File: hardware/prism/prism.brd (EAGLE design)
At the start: 100 x 79 mm, 174 parts, among them IC1 XMEGA128-A1, IC2 74LVC4245APW, IC3 LM2731XMF, IC4 74LVC4245APW, IC5 LM25011MY, IC6 NCV78M05BDTRKG, IC7 NRF24L01+, IC8 MAX3232CSE, T1 MMBT2222LT1G, T2 NTGS4111PT1G, T3 MMBT2222LT1G, T4 MMBT2222LT1G, T5 NTGS4111PT1G, T6 MMBT2222LT1G, T7 MMBT2222LT1G, T8 NTGS4111PT1G

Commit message: few changes on board
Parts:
- added R74, R75: 270-E, robotter_resistor:R0805
- R29, R34: value 4K7-E -> 8K2-E
- R36, R41: value nc -> 3K09-F; device rcl:R0603 -> robotter_resistor:R0603
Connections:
- net +3V3: now also R74.2, R75.2
- net IR_SENSOR_0_OUTPUT_3V3: now also R74.1
- net IR_SENSOR_1_OUTPUT_3V3: now also R75.1
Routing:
- net +3V3: track 398.1 -> 401.1 mm, vias 23 -> 24
- net INT0_0_3V3: track 32.4 -> 31.5 mm
- net INT1_0_3V3: track 30.8 -> 30.2 mm
- net INT0_1_3V3: track 31.3 -> 30.7 mm
- net IR_SENSOR_1_OUTPUT_3V3: track 125.6 -> 126.2 mm

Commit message: mouser component ref added
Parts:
- IC6: device linear:DPACK_3 -> robotter_ic:DPACK_3
- MOT0, MOT1: device con-molex:6410-02 -> robotter_connector:6410-02

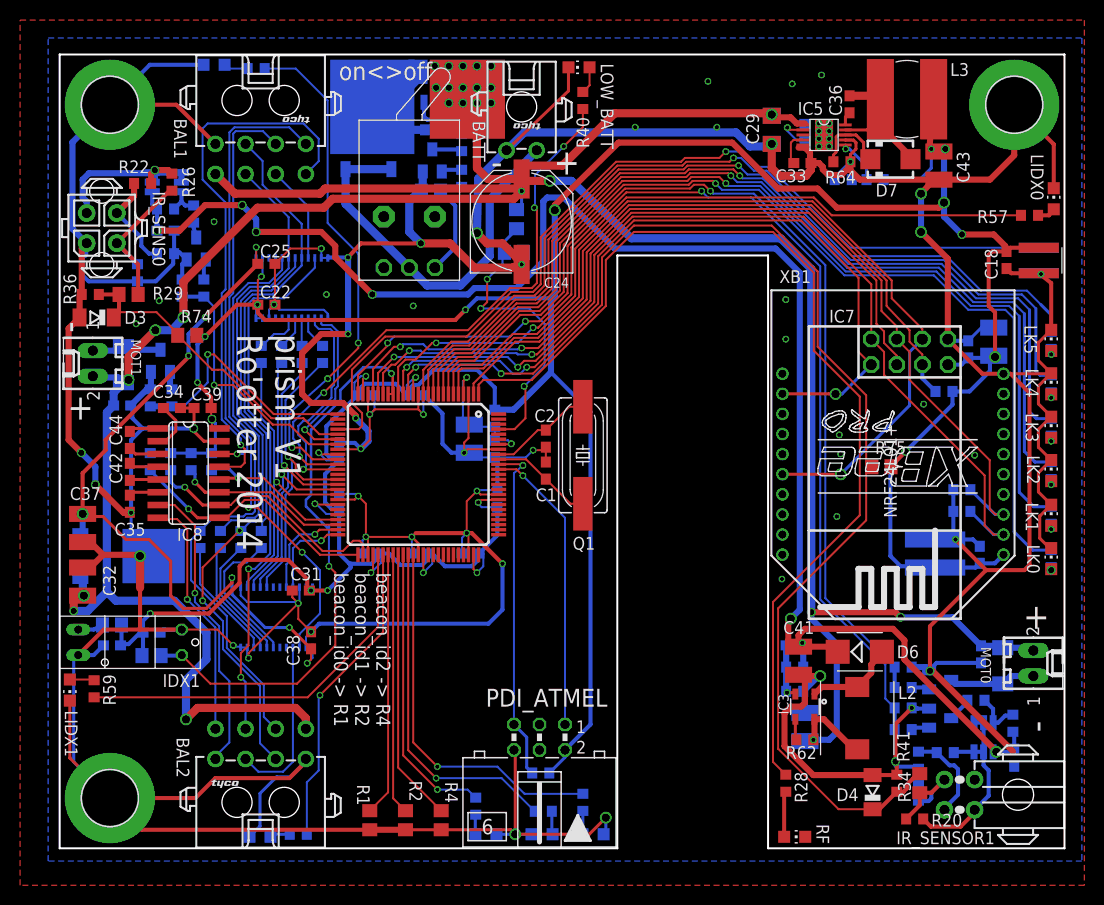
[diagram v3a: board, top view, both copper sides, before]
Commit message: prism v2 : modifications after beacon integration : mirror motor supplied by vbat or +15V, diode B160 pinout corrected
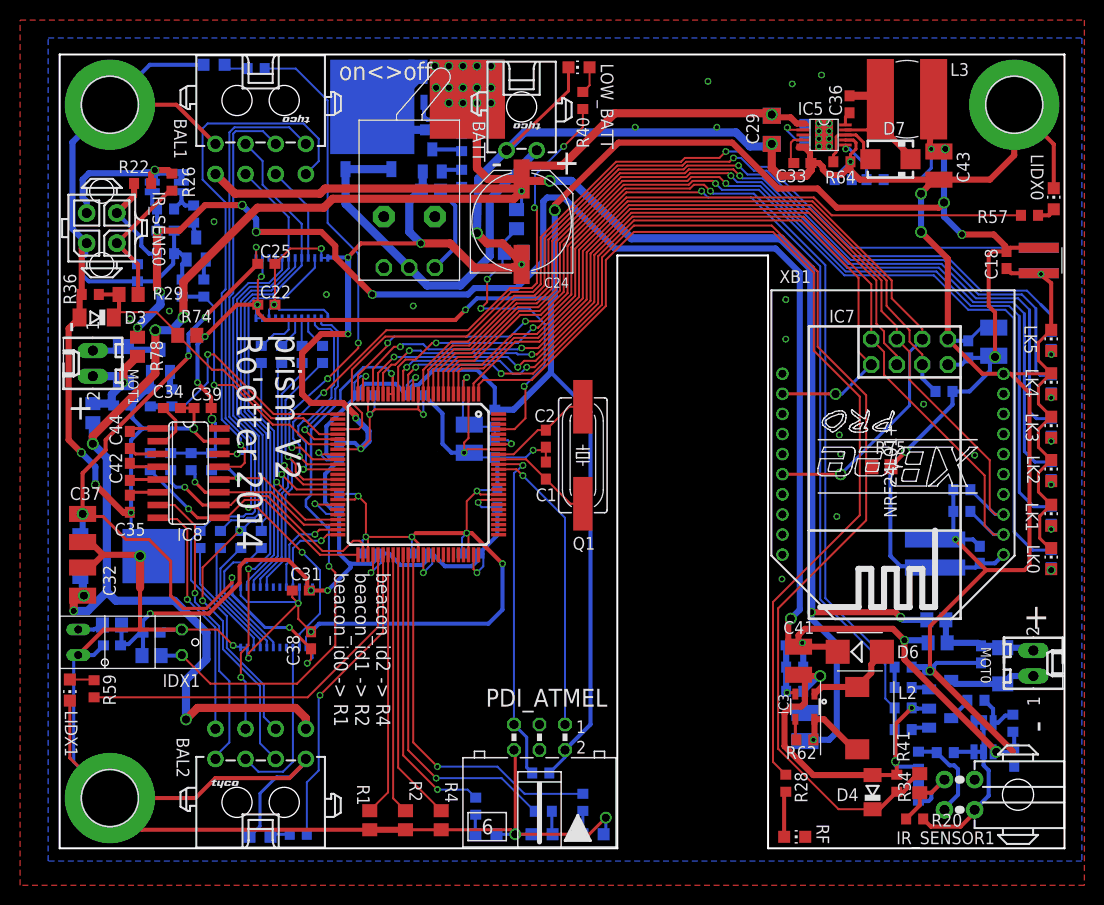
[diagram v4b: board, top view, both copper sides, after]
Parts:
- added R76, R77, R78, R79: 0-E, robotter_resistor:R0805
- turned D7 to 180 degrees
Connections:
- new net VCC_MOT0: C7.1, D2.C, MOT0.2, R76.2, R77.2
- new net VCC_MOT1: C6.1, D1.C, MOT1.2, R78.2, R79.2
- net +15V: now also R77.1, R78.1
- net N$38: now also D7.C; no longer D7.A
- net N$39: now also D7.A; no longer D7.C
- net VBAT: now also R76.1, R79.1; no longer C6.1, C7.1, D1.C, D2.C, MOT0.2, MOT1.2
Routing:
- net +15V: track 161.7 -> 176.0 mm, vias 7 -> 10
- net VBAT: track 344.8 -> 332.2 mm
- net VCC_MOT1: track 0.00 -> 11.2 mm, vias 0 -> 1
- net VCC_MOT0: track 0.00 -> 11.2 mm
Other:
- board text added: "prism_V2 Ro'otter 2014"
- board text removed: "prism_V1 Ro'otter 2014"
